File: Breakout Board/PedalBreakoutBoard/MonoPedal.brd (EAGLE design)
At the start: 100 x 80 mm, 52 parts, among them IC1 LD1117V, IC2 MCP6004P, U1 OPA1652AID

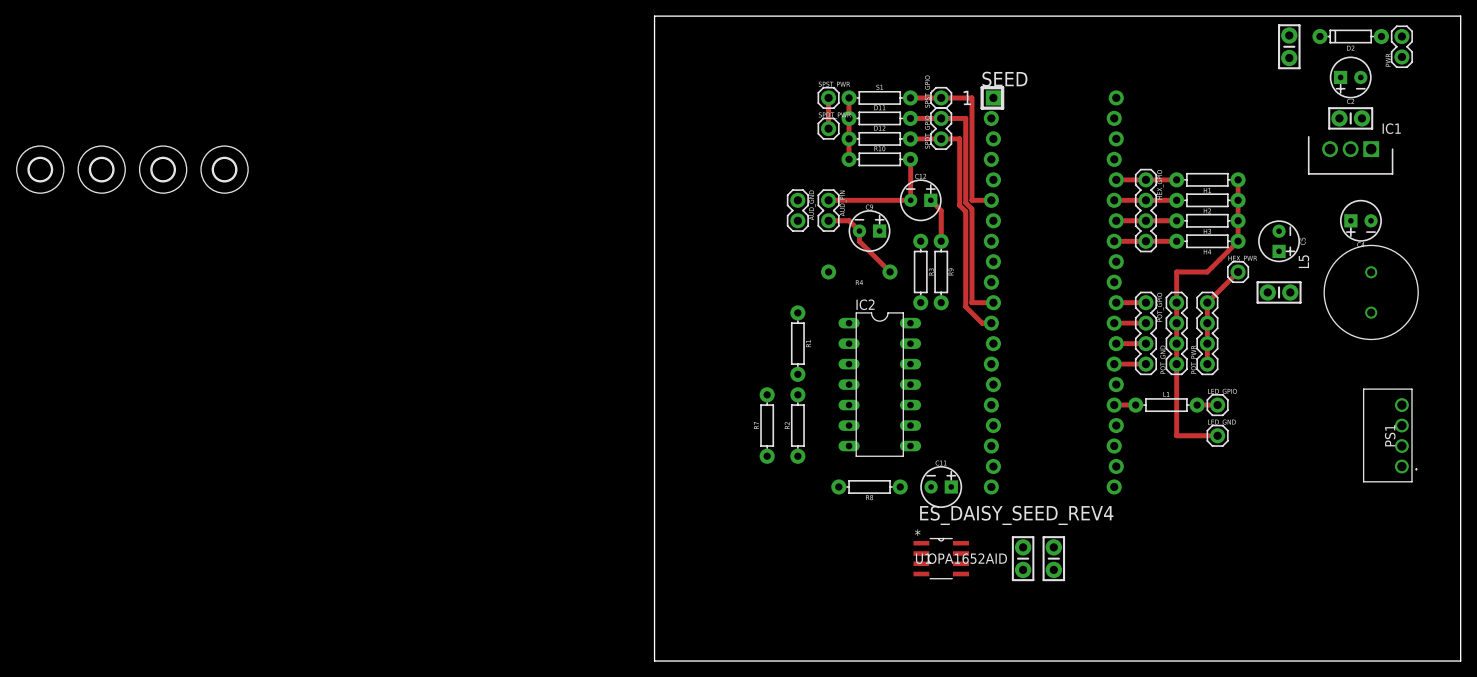
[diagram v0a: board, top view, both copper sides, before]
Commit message: DP-34 - Working on board layout
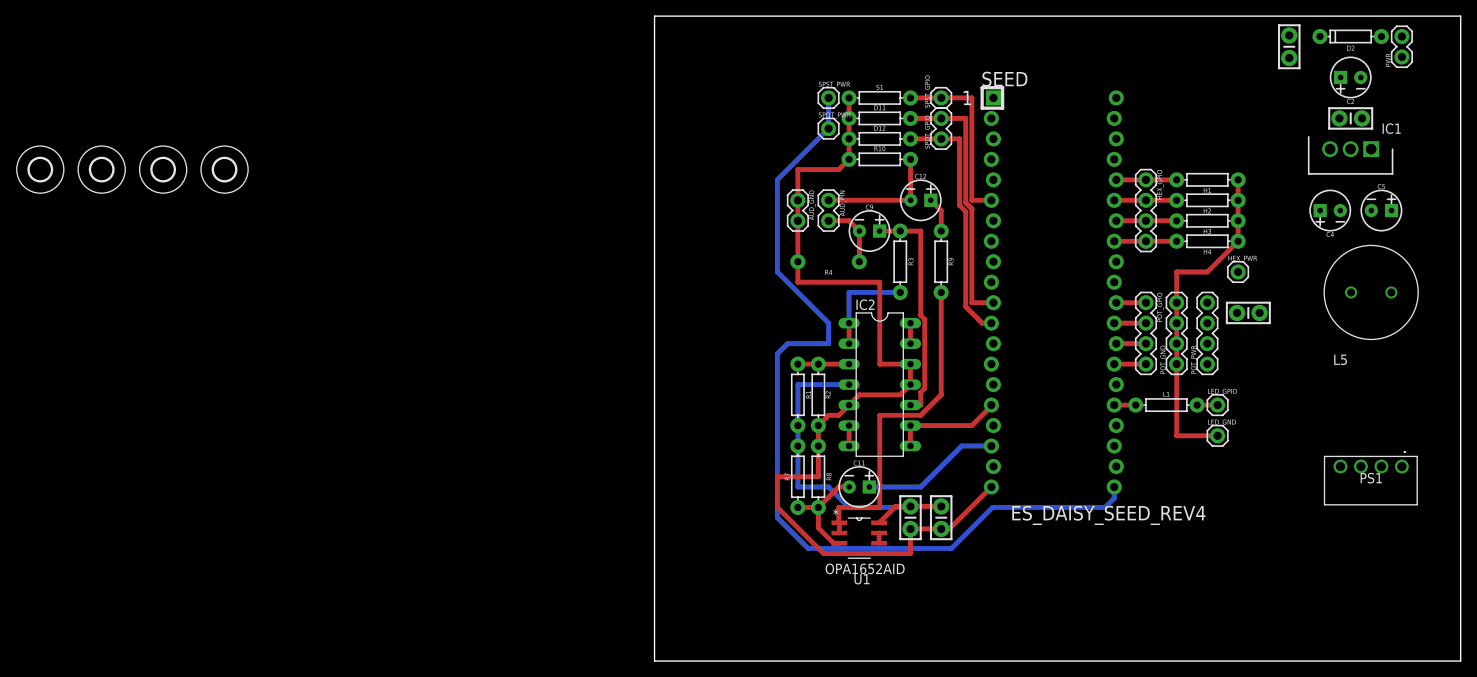
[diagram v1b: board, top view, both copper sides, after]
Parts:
- moved C7 14.9 mm to (31.8, 17.8)
- moved C8 14.9 mm to (35.6, 17.8)
- moved C5 13.3 mm to (90.2, 55.9), turned to 0 degrees
- moved U1 10.5 mm to (25.4, 15.2)
- moved C11 10.2 mm to (25.4, 21.6)
- moved R7 7.41 mm to (17.8, 22.9)
- moved R8 6.48 mm to (20.3, 22.9), turned to 270 degrees
- moved R1 6.35 mm to (17.8, 33.0)
- moved C6 4.58 mm to (73.7, 43.2)
- moved R2 4.58 mm to (20.3, 33.0)
- moved C4 4.02 mm to (83.8, 55.9)
- moved R4 4.02 mm to (21.6, 49.5)
- moved R3 2.84 mm to (30.5, 49.5)
- moved R9 1.27 mm to (35.6, 49.5)
- turned L5 to 0 degrees
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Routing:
- net GND: track 49.8 -> 160.2 mm
- net +3V3_A: track 16.8 -> 110.3 mm
- net +5V_ISOL: track 0.00 -> 42.7 mm
- net N$13: track 0.00 -> 41.1 mm
- net N$9: track 0.00 -> 28.4 mm
- net OUT_L: track 0.00 -> 17.2 mm
- net IN_L: track 0.00 -> 13.7 mm
- net N$12: track 0.00 -> 13.4 mm
- net V_AUDIOBIAS: track 0.00 -> 12.7 mm
- net N$6: track 0.00 -> 6.35 mm
- net IN_L_JACK: track 11.0 -> 8.17 mm
- net N$18: track 0.00 -> 2.54 mm
- net N$10: track 0.00 -> 2.54 mm
- net N$14: track 5.61 -> 4.34 mm
- net N$15: track 0.00 -> 1.27 mm

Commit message: Working on board layout
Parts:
- moved H7 142.7 mm to (62.2, 3.81)
- moved H6 123.2 mm to (62.2, 57.1)
- moved H5 80.8 mm to (3.81, 3.81)
- moved H8 80.1 mm to (3.81, 57.1)
- moved D2 46.6 mm to (45.7, 54.6), turned to 270 degrees
- moved PWR 45.0 mm to (50.8, 58.4), turned to 180 degrees
- moved PS1 42.7 mm to (53.3, 7.62)
- moved C1 42.3 mm to (43.2, 53.3), turned to 90 degrees
- moved C2 42.1 mm to (49.5, 52.1)
- moved L5 39.7 mm to (58.4, 20.3)
- moved C5 39.6 mm to (61.0, 29.2)
- moved C3 34.7 mm to (54.6, 53.3), turned to 90 degrees
- moved IC1 34.7 mm to (58.4, 47.0), turned to 270 degrees
- moved C4 31.5 mm to (59.7, 35.6)
- moved R10 25.7 mm to (6.35, 48.3)
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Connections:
- removed net +3V3_D: SEED.38
- removed net LED2: SEED.24
- removed net LED3: SEED.23
- removed net LED4: SEED.22
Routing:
- net GND: track 160.2 -> 246.1 mm, vias 0 -> 2
- net +5V_ISOL: track 42.7 -> 88.3 mm
- net +9V_IN: track 0.00 -> 38.5 mm
- net N$8: track 0.00 -> 30.8 mm
- net N$7: track 0.00 -> 26.3 mm
- net OUT_L: track 17.2 -> 43.3 mm
- net SPDT1_1: track 32.7 -> 13.0 mm
- net N$12: track 13.4 -> 25.6 mm
- net SPST1: track 22.7 -> 29.6 mm
- net N$6: track 6.35 -> 13.0 mm
- net N$13: track 41.1 -> 34.5 mm, vias 0 -> 1
- net IN_L: track 13.7 -> 8.62 mm
- net V_AUDIOBIAS: track 12.7 -> 7.93 mm
- net SPDT1_2: track 31.3 -> 26.9 mm
- net +3V3_A: track 110.3 -> 114.0 mm
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- added copper zone on layer 1, net GND
- added copper zone on layer 16, net GND
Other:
- board size 100 x 80 mm -> 65.7 x 61 mm

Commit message: DP-34 - First draft board layout complete
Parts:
- moved LED_GPIO 2.54 mm to (49.5, 14.0), turned to 0 degrees
- moved LED_GND 2.54 mm to (47.0, 14.0), turned to 180 degrees
- moved SPDT_PWR 2.54 mm to (11.4, 58.4)
- moved PS1 1.27 mm to (53.3, 6.35)
- moved L5 1.27 mm to (58.4, 21.6)
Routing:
- net SPDT1_1: track 13.0 -> 28.8 mm
- net +3V3_A: track 114.0 -> 111.5 mm
- net N$1: track 2.54 -> 5.08 mm
- net GND: track 246.1 -> 244.3 mm
- net N$7: track 26.3 -> 27.6 mm
- net +5V_ISOL: track 88.3 -> 89.0 mm
- net N$8: track 30.8 -> 30.2 mm
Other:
- board text added: "Mono Pedal REV: B"
- board text added: "Saved By Grace Software"

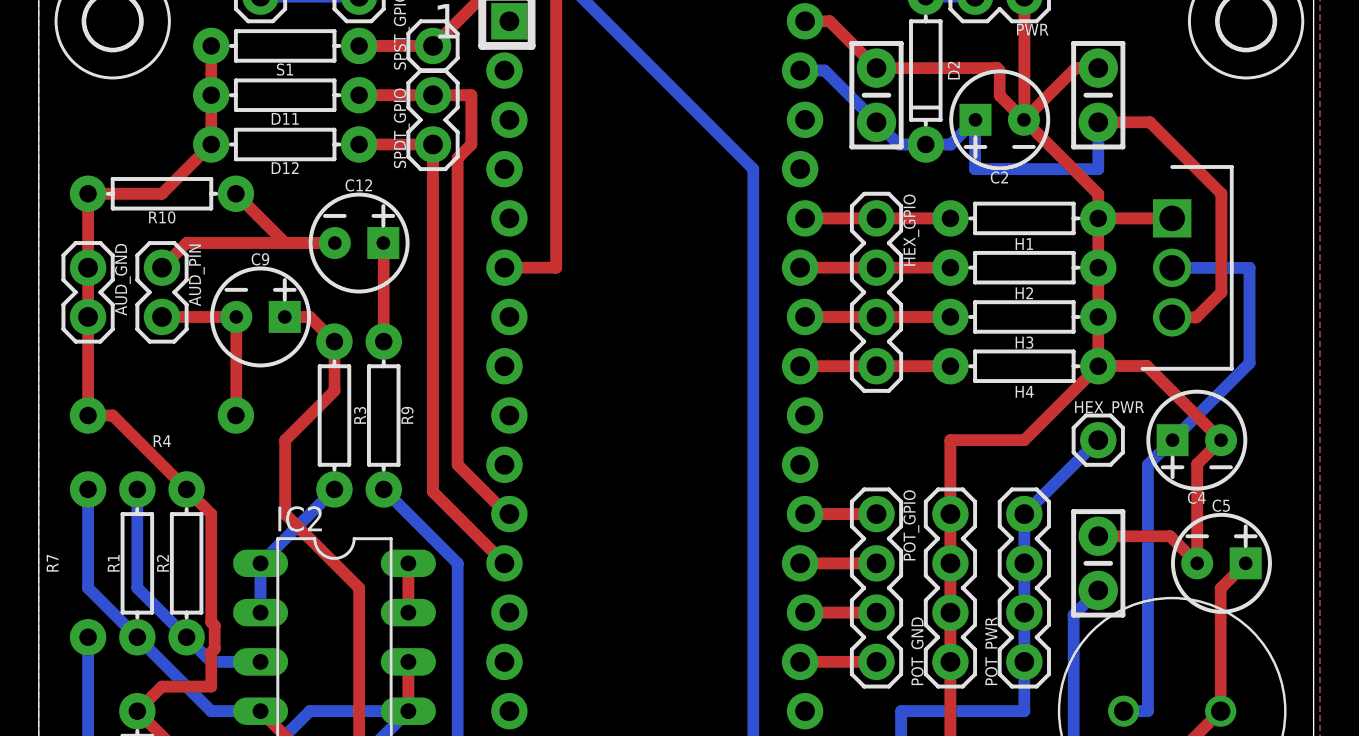
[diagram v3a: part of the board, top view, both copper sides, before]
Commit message: DP-34 - Fixing silk screen errors
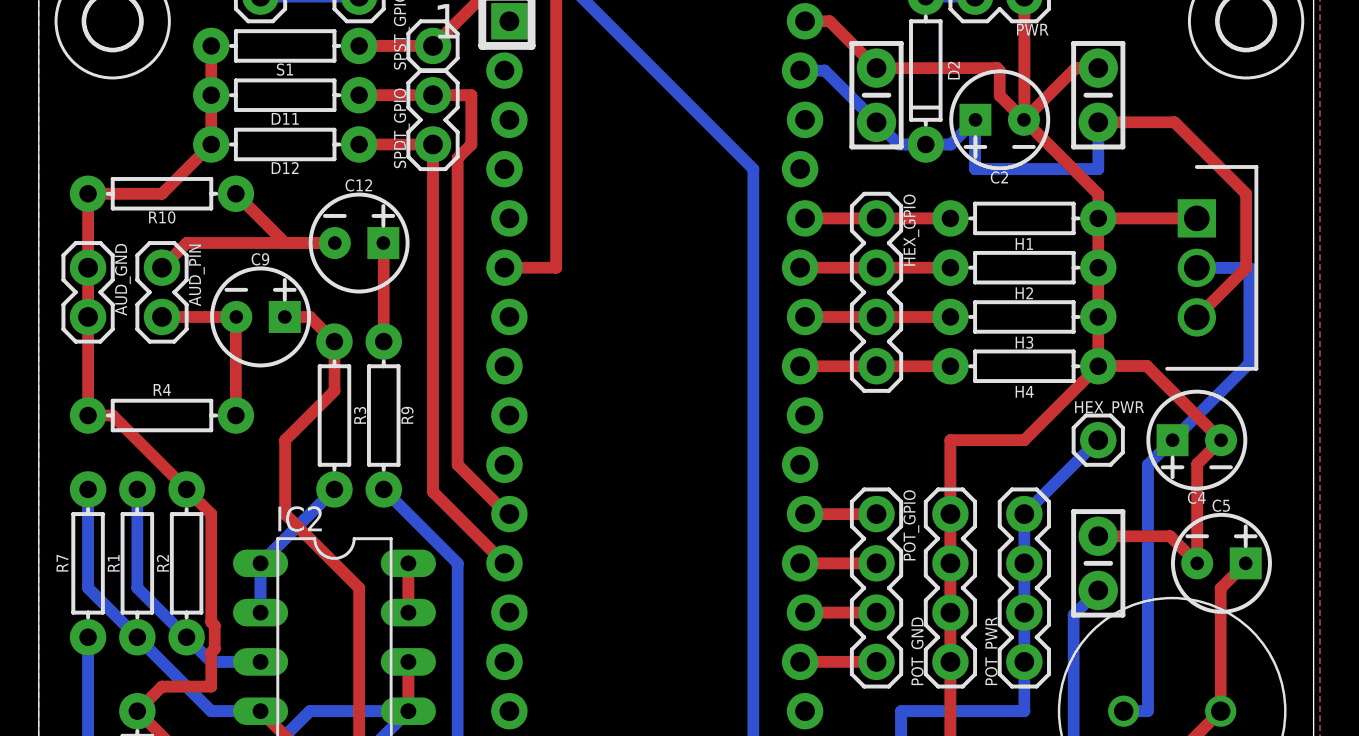
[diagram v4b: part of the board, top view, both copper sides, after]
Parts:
- moved IC1 1.27 mm to (59.7, 47.0)
- flipped R4 to the top, turned to 0 degrees
- flipped R7 to the top
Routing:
- net GND: track 244.3 -> 245.6 mm
- net N$8: track 30.2 -> 29.0 mm
- net +9V_IN: track 38.5 -> 39.0 mm
